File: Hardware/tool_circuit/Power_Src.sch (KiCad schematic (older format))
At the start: 0 parts

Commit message: Pi hat
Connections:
- net labels added: VDC
- net labels removed: +3.3V
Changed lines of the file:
@@
 $Descr A4 11693 8268
 encoding utf-8
-Sheet 5 5
+Sheet 6 6
 Title ""
 Date ""
@@
 $EndComp
 $Comp
-L power:+3.3V #PWR?
-U 1 1 611EFC98
-P 6150 1800
-F 0 "#PWR?" H 6150 1650 50  0001 C CNN
-F 1 "+3.3V" H 6165 1973 50  0000 C CNN
-F 2 "" H 6150 1800 50  0001 C CNN
-F 3 "" H 6150 1800 50  0001 C CNN
-	1    6150 1800
+L power:VDC #PWR?
+U 1 1 612B15A0
+P 4800 1900
+F 0 "#PWR?" H 4800 1800 50  0001 C CNN
+F 1 "VDC" H 4815 2073 50  0000 C CNN
+F 2 "" H 4800 1900 50  0001 C CNN
+F 3 "" H 4800 1900 50  0001 C CNN
+	1    4800 1900
 	1    0    0    -1
 $EndComp

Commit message: regulator/other changes
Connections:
- net labels added: 5V
- net labels removed: VDC
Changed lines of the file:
@@
 $Descr A4 11693 8268
 encoding utf-8
-Sheet 6 6
+Sheet 6 7
 Title ""
 Date ""
@@
 L power:+BATT #PWR?
 U 1 1 611ECA0B
-P 4000 1850
-F 0 "#PWR?" H 4000 1700 50  0001 C CNN
-F 1 "+BATT" H 4015 2023 50  0000 C CNN
-F 2 "" H 4000 1850 50  0001 C CNN
-F 3 "" H 4000 1850 50  0001 C CNN
-	1    4000 1850
+P 2750 1950
+F 0 "#PWR?" H 2750 1800 50  0001 C CNN
+F 1 "+BATT" H 2765 2123 50  0000 C CNN
+F 2 "" H 2750 1950 50  0001 C CNN
+F 3 "" H 2750 1950 50  0001 C CNN
+	1    2750 1950
 	1    0    0    -1
 $EndComp
-$Comp
-L power:VDC #PWR?
-U 1 1 612B15A0
-P 4800 1900
-F 0 "#PWR?" H 4800 1800 50  0001 C CNN
-F 1 "VDC" H 4815 2073 50  0000 C CNN
-F 2 "" H 4800 1900 50  0001 C CNN
-F 3 "" H 4800 1900 50  0001 C CNN
-	1    4800 1900
-	1    0    0    -1
-$EndComp
+Text HLabel 6700 2950 0    50   Output ~ 0
+5V
+$Sheet
+S 5150 2300 1550 900
+U 6131D12D
+F0 "5V Regulator" 50
+F1 "5V Regulator.sch" 50
+$EndSheet
 $EndSCHEMATC

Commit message: 5v regulator
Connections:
- wire segments 0 -> 1
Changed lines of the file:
@@
 L power:+BATT #PWR?
 U 1 1 611ECA0B
-P 2750 1950
-F 0 "#PWR?" H 2750 1800 50  0001 C CNN
-F 1 "+BATT" H 2765 2123 50  0000 C CNN
-F 2 "" H 2750 1950 50  0001 C CNN
-F 3 "" H 2750 1950 50  0001 C CNN
-	1    2750 1950
+P 4150 2500
+F 0 "#PWR?" H 4150 2350 50  0001 C CNN
+F 1 "+BATT" H 4165 2673 50  0000 C CNN
+F 2 "" H 4150 2500 50  0001 C CNN
+F 3 "" H 4150 2500 50  0001 C CNN
+	1    4150 2500
 	1    0    0    -1
 $EndComp
@@
 F1 "5V Regulator.sch" 50
 $EndSheet
+Wire Wire Line
+	4150 2500 5150 2500
 $EndSCHEMATC

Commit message: symbols
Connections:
- net labels added: 12V_BATTERY
- net labels removed: +BATT
- wire segments 1 -> 0
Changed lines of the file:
@@
 $Descr A4 11693 8268
 encoding utf-8
-Sheet 6 7
+Sheet 4 5
 Title ""
 Date ""
@@
 Comment4 ""
 $EndDescr
-$Comp
-L power:+BATT #PWR?
-U 1 1 611ECA0B
-P 4150 2500
-F 0 "#PWR?" H 4150 2350 50  0001 C CNN
-F 1 "+BATT" H 4165 2673 50  0000 C CNN
-F 2 "" H 4150 2500 50  0001 C CNN
-F 3 "" H 4150 2500 50  0001 C CNN
-	1    4150 2500
-	1    0    0    -1
-$EndComp
 Text HLabel 6700 2950 0    50   Output ~ 0
 5V
@@
 F1 "5V Regulator.sch" 50
 $EndSheet
-Wire Wire Line
-	4150 2500 5150 2500
+Text HLabel 5150 2450 0    50   Input ~ 0
+12V_BATTERY
 $EndSCHEMATC

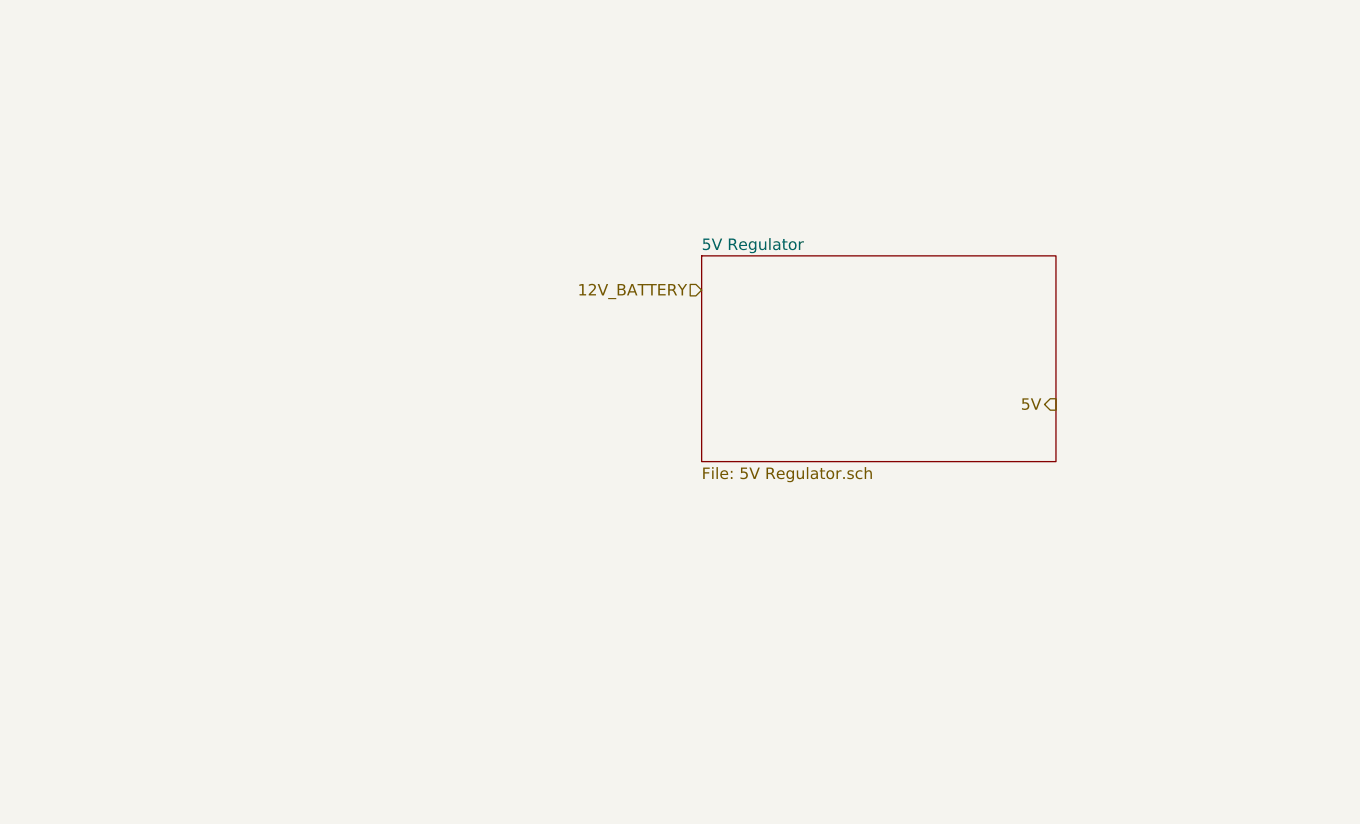
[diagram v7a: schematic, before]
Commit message: Tool Circuit schematic updates
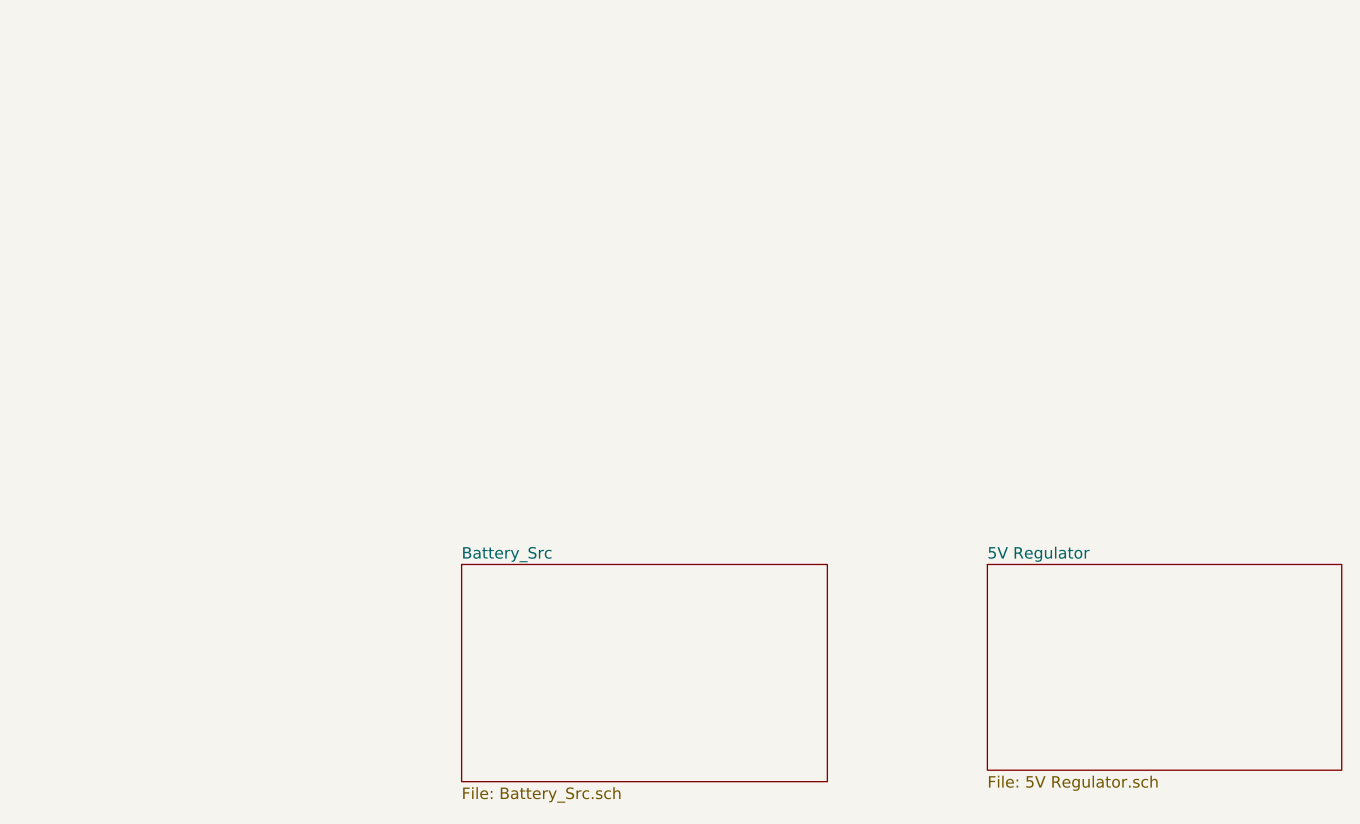
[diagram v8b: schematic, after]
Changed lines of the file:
@@
 $Descr A4 11693 8268
 encoding utf-8
-Sheet 3 7
+Sheet 2 8
 Title ""
 Date ""
@@
 Comment4 ""
 $EndDescr
-Text HLabel 6700 2950 0    50   Output ~ 0
-5V
 $Sheet
-S 5150 2300 1550 900
+S 6400 3650 1550 900
 U 6131D12D
 F0 "5V Regulator" 50
 F1 "5V Regulator.sch" 50
 $EndSheet
-Text HLabel 5150 2450 0    50   Input ~ 0
-12V_BATTERY
+$Sheet
+S 4100 3650 1600 950
+U 614E4070
+F0 "Battery_Src" 50
+F1 "Battery_Src.sch" 50
+$EndSheet
 $EndSCHEMATC
